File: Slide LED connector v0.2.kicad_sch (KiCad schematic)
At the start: 18 parts, among them SW1 SW_Push, SW2 SW_Push, U5 ESP32-WROOM-32U

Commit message: MOAR STITCHING and some cleanup
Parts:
- added TP7: TestPoint, TestPoint:TestPoint_Pad_D2.0mm, symbol Connector:TestPoint
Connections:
- net GND: now also TP7.1

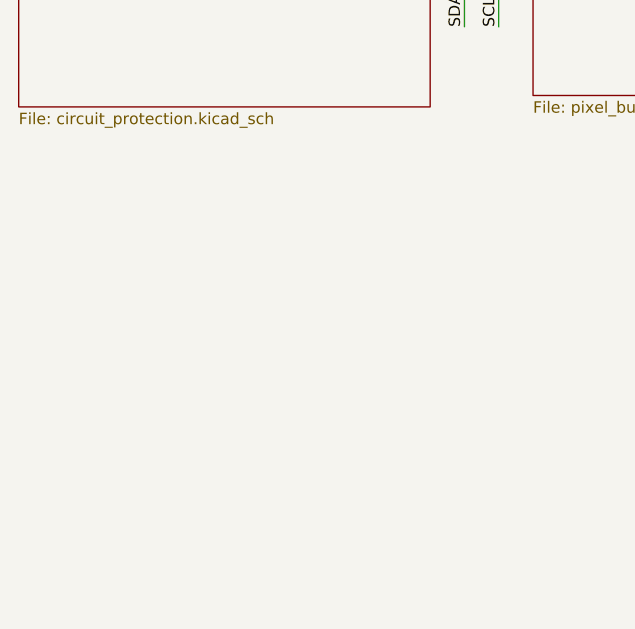
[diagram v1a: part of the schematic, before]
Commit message: added power diagram
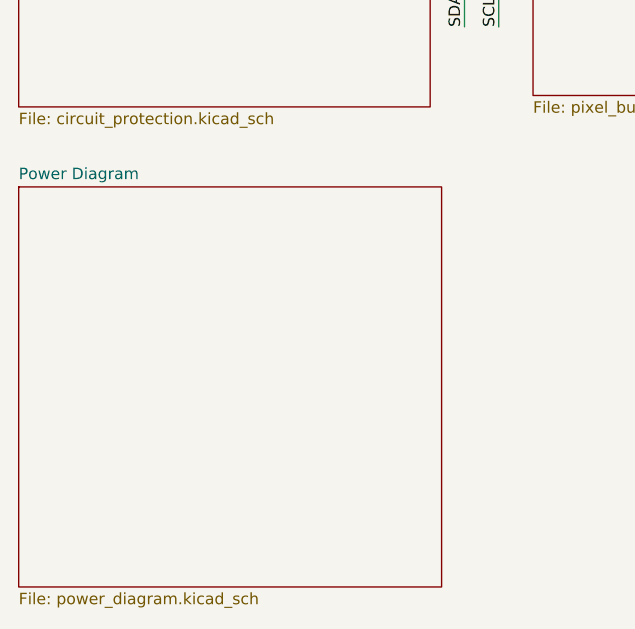
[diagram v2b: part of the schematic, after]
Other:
- added sheet Power Diagram (power_diagram.kicad_sch)
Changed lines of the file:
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@@
+	)
+	(sheet
+		(at 17.78 144.78)
+		(size 46.99 44.45)
+		(exclude_from_sim no)
+		(in_bom yes)
+		(on_board yes)
+		(dnp no)
+		(fields_autoplaced yes)
+		(stroke
+			(width 0.1524)
+			(type solid)
+		)
+		(fill
+			(color 0 0 0 0.0000)
+		)
+		(property "Sheetname" "Power Diagram"
+			(at 17.78 144.0684 0)
+			(effects
+				(font
+					(size 1.27 1.27)
+				)
+				(justify left bottom)
+			)
+		)
+		(property "Sheetfile" "power_diagram.kicad_sch"
+			(at 17.78 189.8146 0)
+			(effects
+				(font
+					(size 1.27 1.27)
+				)
+				(justify left top)
+			)
+		)
+		(instances
+			(project "Slide LED connector v0.2"
+				(path "/bf4b09fd-2d42-43b2-9834-c05987d36a77"
+					(page "17")
+				)
+			)
+		)
 	)
 	(sheet
